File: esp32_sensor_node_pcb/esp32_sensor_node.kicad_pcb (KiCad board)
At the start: 4 copper layers, 49.9 x 59.9 mm, 28 parts, among them J1 Conn_02x10_Odd_Even, Q1 2N7002K, SW1 SW_DIP_x01, SW2 SW_DIP_x01, U1 SPX3819M5-L-3-3, U2 ESP32-WROOM-E, U3 MAX3483AEASA+

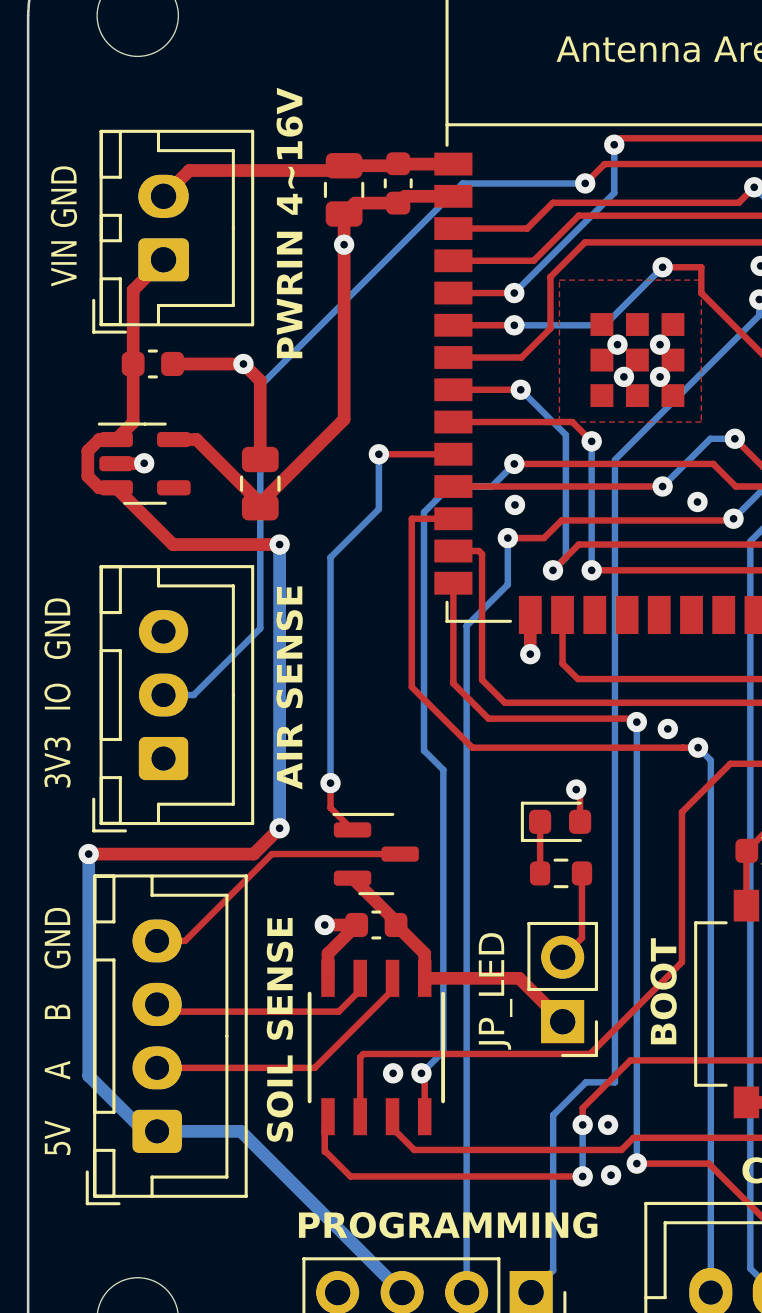
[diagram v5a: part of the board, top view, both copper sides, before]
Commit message: Add fab files. Add dot next to MAX3843 to indicate pin1
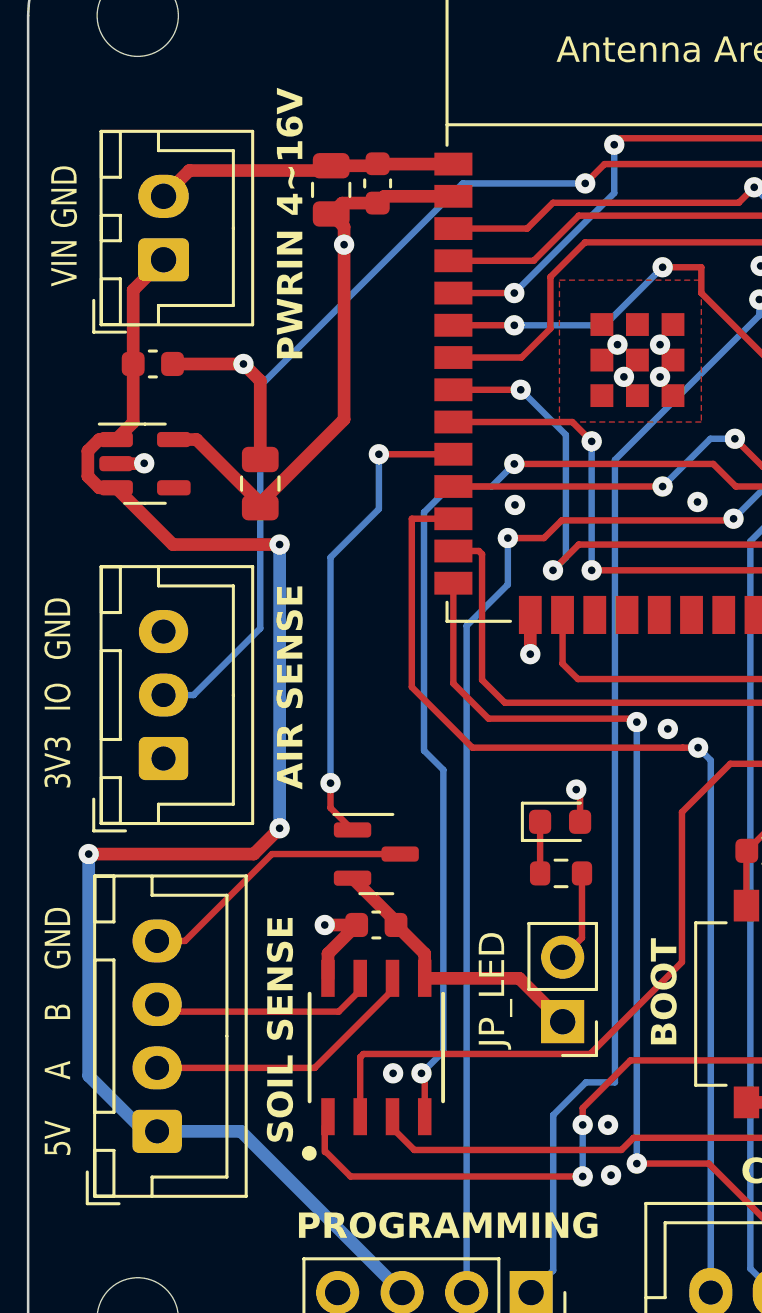
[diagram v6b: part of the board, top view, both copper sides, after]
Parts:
- moved C3 0.81 mm to (33.8, 31.0)
- moved C4 0.51 mm to (32.0, 31.2)
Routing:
- net +3.3V: track 27.8 -> 28.5 mm
- net GND: track 60.0 -> 60.5 mm
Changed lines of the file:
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@@
       (usegerberattributes true)
       (usegerberadvancedattributes true)
-      (creategerberjobfile true)
+      (creategerberjobfile false)
       (dashed_line_dash_ratio 12.000000)
       (dashed_line_gap_ratio 3.000000)
@@
       (psnegative false)
       (psa4output false)
-      (plotreference true)
-      (plotvalue true)
+      (plotreference false)
+      (plotvalue false)
       (plotinvisibletext false)
       (sketchpadsonfab false)
@@
       (drillshape 0)
       (scaleselection 1)
-      (outputdirectory "")
+      (outputdirectory "Fab/")
     )
   )
@@
   )
   (footprint "Capacitor_SMD:C_0805_2012Metric" (layer "F.Cu")
-    (at 32.512 31.242 90)
+    (at 32.004 31.242 90)
     (descr "Capacitor SMD 0805 (2012 Metric), square (rectangular) end terminal, IPC_7351 nominal, (Body size source: IPC-SM-782 page 76, https://www.pcb-3d.com/wordpress/wp-content/uploads/ipc-sm-782a_amendment_1_and_2.pdf, https://docs.google.com/spreadsheets/d/1BsfQQcO9C6DZCsRaXUlFlo91Tg2WpOkGARC1WS5S8t0/edit?usp=sharing), generated with kicad-footprint-generator")
     (tags "capacitor")
@@
   )
   (footprint "Capacitor_SMD:C_0603_1608Metric" (layer "F.Cu")
-    (at 34.644 30.988 90)
+    (at 33.8328 30.988 90)
     (descr "Capacitor SMD 0603 (1608 Metric), square (rectangular) end terminal, IPC_7351 nominal, (Body size source: IPC-SM-782 page 76, https://www.pcb-3d.com/wordpress/wp-content/uploads/ipc-sm-782a_amendment_1_and_2.pdf), generated with kicad-footprint-generator")
     (tags "capacitor")
@@
     )
     (stroke (width 0.15) (type solid)) (fill solid) (layer "F.SilkS"))
+  (gr_circle (center 31.1404 69.1896) (end 31.355926 69.1896)
+    (stroke (width 0.15) (type solid)) (fill solid) (layer "F.SilkS"))
   (gr_rect (start 68.707 51.054) (end 69.215 55.9308)
     (stroke (width 0.15) (type solid)) (fill solid) (layer "F.SilkS"))
@@
   (segment (start 22.452 66.14) (end 22.452 57.404) (width 0.5) (layer "B.Cu") (net 1))
   (segment (start 34.684 74.435) (end 34.684 74.676) (width 0.5) (layer "B.Cu") (net 1))
+  (segment (start 32.433 31.763) (end 32.004 32.192) (width 0.5) (layer "F.Cu") (net 2))
+  (segment (start 34.0998 31.496) (end 36.816 31.496) (width 0.5) (layer "F.Cu") (net 2))
+  (segment (start 33.8328 31.763) (end 32.433 31.763) (width 0.5) (layer "F.Cu") (net 2))
   (segment (start 26.6998 41.0768) (end 29.21 43.587) (width 0.5) (layer "F.Cu") (net 2))
-  (segment (start 32.512 32.192) (end 32.512 33.401) (width 0.5) (layer "F.Cu") (net 2))
   (segment (start 41.807 55.015) (end 41.656 54.864) (width 0.254) (layer "F.Cu") (net 2))
   (segment (start 41.807 56.134) (end 41.807 55.015) (width 0.254) (layer "F.Cu") (net 2))
@@
   (segment (start 29.21 43.587) (end 32.512 40.285) (width 0.5) (layer "F.Cu") (net 2))
   (segment (start 31.877 62.29985) (end 31.877 61.328) (width 0.5) (layer "F.Cu") (net 2))
-  (segment (start 34.911 31.496) (end 36.816 31.496) (width 0.5) (layer "F.Cu") (net 2))
   (segment (start 32.512 40.285) (end 32.512 33.401) (width 0.5) (layer "F.Cu") (net 2))
   (segment (start 31.75 60.198) (end 33.007 60.198) (width 0.5) (layer "F.Cu") (net 2))
+  (segment (start 32.004 32.192) (end 32.512 32.7) (width 0.5) (layer "F.Cu") (net 2))
   (segment (start 31.877 61.328) (end 33.007 60.198) (width 0.5) (layer "F.Cu") (net 2))
-  (segment (start 32.941 31.763) (end 32.512 32.192) (width 0.5) (layer "F.Cu") (net 2))
   (segment (start 55.472 54.8026) (end 55.472 55.499) (width 0.5) (layer "F.Cu") (net 2))
-  (segment (start 34.644 31.763) (end 34.911 31.496) (width 0.5) (layer "F.Cu") (net 2))
   (segment (start 25.8064 41.0768) (end 26.6998 41.0768) (width 0.5) (layer "F.Cu") (net 2))
-  (segment (start 34.644 31.763) (end 32.941 31.763) (width 0.5) (layer "F.Cu") (net 2))
+  (segment (start 32.512 32.7) (end 32.512 33.401) (width 0.5) (layer "F.Cu") (net 2))
+  (segment (start 33.8328 31.763) (end 34.0998 31.496) (width 0.5) (layer "F.Cu") (net 2))
   (via (at 31.75 60.198) (size 0.8) (drill 0.3) (layers "F.Cu" "B.Cu") (net 2))
   (via (at 55.472 55.499) (size 0.8) (drill 0.3) (layers "F.Cu" "B.Cu") (net 2))
@@
   (via (at 50.138 53.848) (size 0.8) (drill 0.3) (layers "F.Cu" "B.Cu") (net 25))
   (segment (start 50.138 53.848) (end 50.138 49.784) (width 0.254) (layer "B.Cu") (net 25))
-  (segment (start 36.816 30.226) (end 34.657 30.226) (width 0.5) (layer "F.Cu") (net 26))
+  (segment (start 33.8458 30.226) (end 33.8328 30.213) (width 0.5) (layer "F.Cu") (net 26))
   (segment (start 24.6228 42.0268) (end 24.638 42.0116) (width 0.5) (layer "F.Cu") (net 26))
-  (segment (start 34.565 30.292) (end 34.644 30.213) (width 0.5) (layer "F.Cu") (net 26))
-  (segment (start 34.657 30.226) (end 34.644 30.213) (width 0.5) (layer "F.Cu") (net 26))
+  (segment (start 32.004 30.292) (end 33.7538 30.292) (width 0.5) (layer "F.Cu") (net 26))
   (segment (start 51.8245 57.404) (end 54.964 57.404) (width 0.5) (layer "F.Cu") (net 26))
   (segment (start 34.557 60.0665) (end 32.8445 58.354) (width 0.5) (layer "F.Cu") (net 26))
@@
   (segment (start 29.21 38.762) (end 28.548 38.1) (width 0.5) (layer "F.Cu") (net 26))
   (segment (start 54.316 30.226) (end 55.626 30.226) (width 0.5) (layer "F.Cu") (net 26))
+  (segment (start 36.816 30.226) (end 33.8458 30.226) (width 0.5) (layer "F.Cu") (net 26))
   (segment (start 23.5314 42.0268) (end 24.6228 42.0268) (width 0.5) (layer "F.Cu") (net 26))
   (segment (start 50.8085 56.388) (end 51.8245 57.404) (width 0.5) (layer "F.Cu") (net 26))
@@
   (segment (start 39.41285 62.29985) (end 41.121 64.008) (width 0.5) (layer "F.Cu") (net 26))
   (segment (start 39.846 49.53) (end 39.846 47.986) (width 0.5) (layer "F.Cu") (net 26))
+  (segment (start 33.7538 30.292) (end 33.8328 30.213) (width 0.5) (layer "F.Cu") (net 26))
   (segment (start 35.687 62.29985) (end 39.41285 62.29985) (width 0.5) (layer "F.Cu") (net 26))
   (segment (start 48.36 67.186) (end 51.278 67.186) (width 0.5) (layer "F.Cu") (net 26))
@@
   (segment (start 50.8085 56.388) (end 50.8085 56.3925) (width 0.5) (layer "F.Cu") (net 26))
   (segment (start 26.416 30.48) (end 32.324 30.48) (width 0.5) (layer "F.Cu") (net 26))
-  (segment (start 32.512 30.292) (end 34.565 30.292) (width 0.5) (layer "F.Cu") (net 26))
   (via (at 51.7652 52.3748) (size 0.8) (drill 0.3) (layers "F.Cu" "B.Cu") (net 26))
   (via (at 56.4896 53.34) (size 0.8) (drill 0.3) (layers "F.Cu" "B.Cu") (net 26))
